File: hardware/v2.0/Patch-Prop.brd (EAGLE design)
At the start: 50 x 28 mm, 49 parts, among them IC1 TPS77033, IC2 XBEE, IC3 MMA8452Q, IC4 ATMEGA168, IC5 MCP1253, IC6 W2RV005RM, U2 MCP73831, X1 USBSMD

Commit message: More small fixes
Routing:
- net GND: track 204.4 -> 234.0 mm
- net VIBE_CONTROL: track 30.5 -> 29.8 mm
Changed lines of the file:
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@@
 <wire x1="44.75" y1="16.2" x2="45.99" y2="14.96" width="0.3048" layer="16"/>
 <wire x1="45.99" y1="14.96" x2="48" y2="14.96" width="0.3048" layer="16"/>
-<wire x1="24.025" y1="11.1" x2="23.6" y2="12.525" width="0" layer="19" extent="16-16"/>
-<wire x1="12.9" y1="20" x2="12.85" y2="20.05" width="0" layer="19" extent="1-16"/>
+<wire x1="8.2" y1="21.7" x2="8.2" y2="19" width="0.3048" layer="1"/>
+<wire x1="8.2" y1="19" x2="8.9" y2="18.3" width="0.3048" layer="1"/>
+<wire x1="8.9" y1="18.3" x2="12.4" y2="18.3" width="0.3048" layer="1"/>
+<wire x1="12.4" y1="18.3" x2="12.9" y2="18.8" width="0.3048" layer="1"/>
+<wire x1="12.9" y1="18.8" x2="12.9" y2="20" width="0.3048" layer="1"/>
+<wire x1="31.2" y1="23.7" x2="15.4" y2="23.7" width="0.3048" layer="1"/>
+<wire x1="15.4" y1="23.7" x2="12.9" y2="21.2" width="0.3048" layer="1"/>
+<wire x1="12.9" y1="21.2" x2="12.9" y2="20" width="0.3048" layer="1"/>
 </signal>
 <signal name="+3V3">
@@
 <wire x1="16.5" y1="26.6" x2="20.3" y2="22.8" width="0.3048" layer="16"/>
 <via x="20.3" y="22.8" extent="1-16" drill="0.5" shape="octagon"/>
-<wire x1="20.3" y1="22.8" x2="20.6" y2="23.1" width="0.3048" layer="1"/>
 <wire x1="29.1" y1="19.9" x2="29.1" y2="22.7" width="0.3048" layer="1"/>
-<wire x1="29.1" y1="22.7" x2="28.4" y2="23.4" width="0.3048" layer="1"/>
-<wire x1="28.4" y1="23.4" x2="20.9" y2="23.4" width="0.3048" layer="1"/>
-<wire x1="20.9" y1="23.4" x2="20.3" y2="22.8" width="0.3048" layer="1"/>
 <wire x1="29.1" y1="19.9" x2="32.9" y2="16.1" width="0.3048" layer="1"/>
 <wire x1="32.9" y1="16.1" x2="32.9" y2="13.7" width="0.3048" layer="1"/>
+<wire x1="29.1" y1="22.7" x2="28.7" y2="23.1" width="0.3048" layer="1"/>
+<wire x1="28.7" y1="23.1" x2="20.6" y2="23.1" width="0.3048" layer="1"/>
+<wire x1="20.6" y1="23.1" x2="20.3" y2="22.8" width="0.3048" layer="1"/>
 </signal>
 <signal name="VIBE">

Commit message: Cleanup
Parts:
- added R10: 4.7k, rcl:R0603
- added R6: RLim, rcl:R0603
- moved R8 17.5 mm to (42.1, 3.40)
- moved R9 15.8 mm to (40.3, 12.9), turned to 270 degrees
- moved C7 5.00 mm to (48.0, 6.00), turned to 270 degrees
- moved T2 2.00 mm to (16.5, 25.5)
- moved SJ2 1.00 mm to (37.2, 5.60), turned to 180 degrees
- moved IC6 0.92 mm to (45.7, 5.40), turned to 270 degrees
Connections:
- new net N$12: IC6.3, R9.1
- new net N$4: R6.2, T2.E
- new net N$7: IC6.1, R8.1
- new net N$9: IC6.2, R10.1
- net +3V3: no longer R8.2, R9.2
- net BLUE: now also R8.2; no longer IC6.1
- net GND: now also R6.1; no longer T2.E
- net GREEN: now also R10.2; no longer IC6.2
- net RED: now also R9.2; no longer IC6.3
- net SCL: no longer R9.1
- net SDA: no longer R8.1
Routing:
- net GND: track 234.0 -> 211.6 mm, vias 7 -> 5
- net RED: track 11.9 -> 4.18 mm
- net BLUE: track 9.66 -> 2.75 mm
- net GREEN: track 9.54 -> 3.45 mm
- net V+: track 81.3 -> 75.9 mm, vias 5 -> 4
- net SDA: track 9.16 -> 5.01 mm
- net N$4: track 0.00 -> 2.87 mm
- net N$1: track 38.3 -> 40.7 mm
- net +3V3: track 132.5 -> 130.4 mm
- net SCL: track 10.7 -> 8.85 mm
- net VIBE: track 9.16 -> 7.45 mm
- net VIBE_CONTROL: track 29.8 -> 28.9 mm

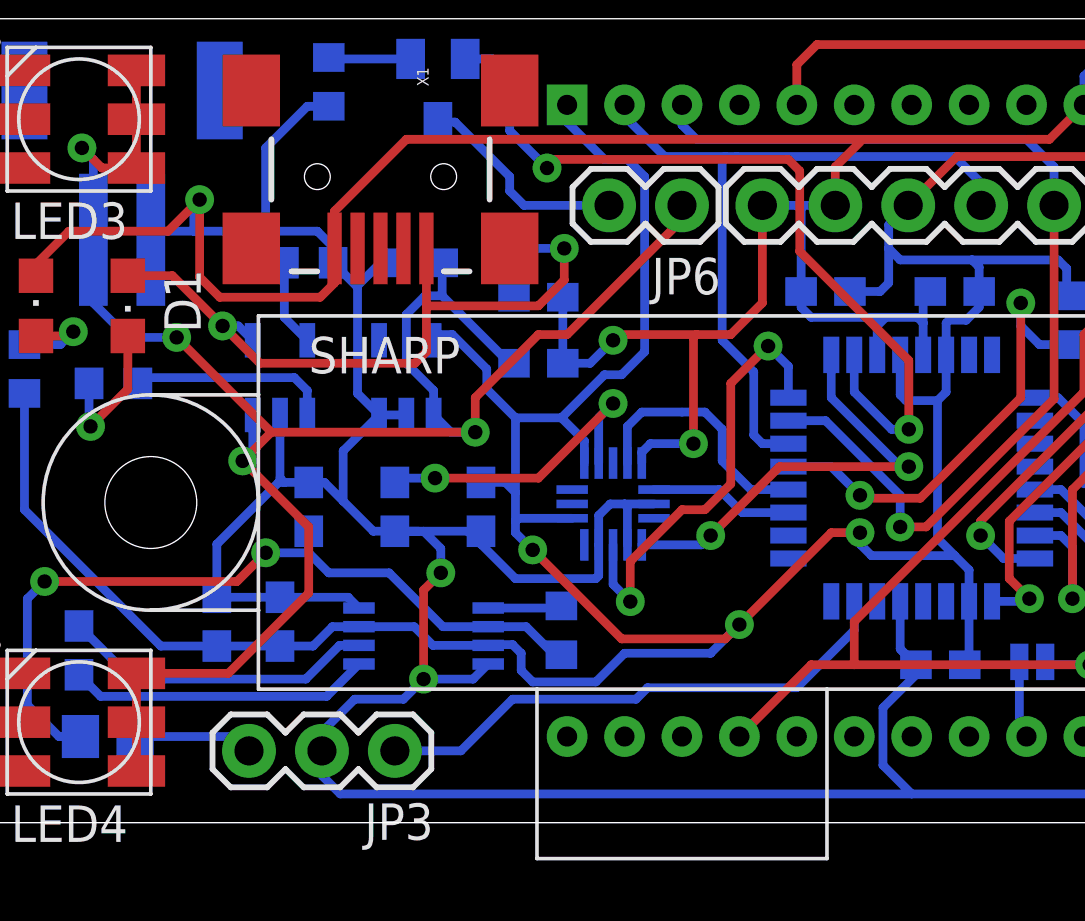
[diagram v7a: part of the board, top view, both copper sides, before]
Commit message: About to move uC
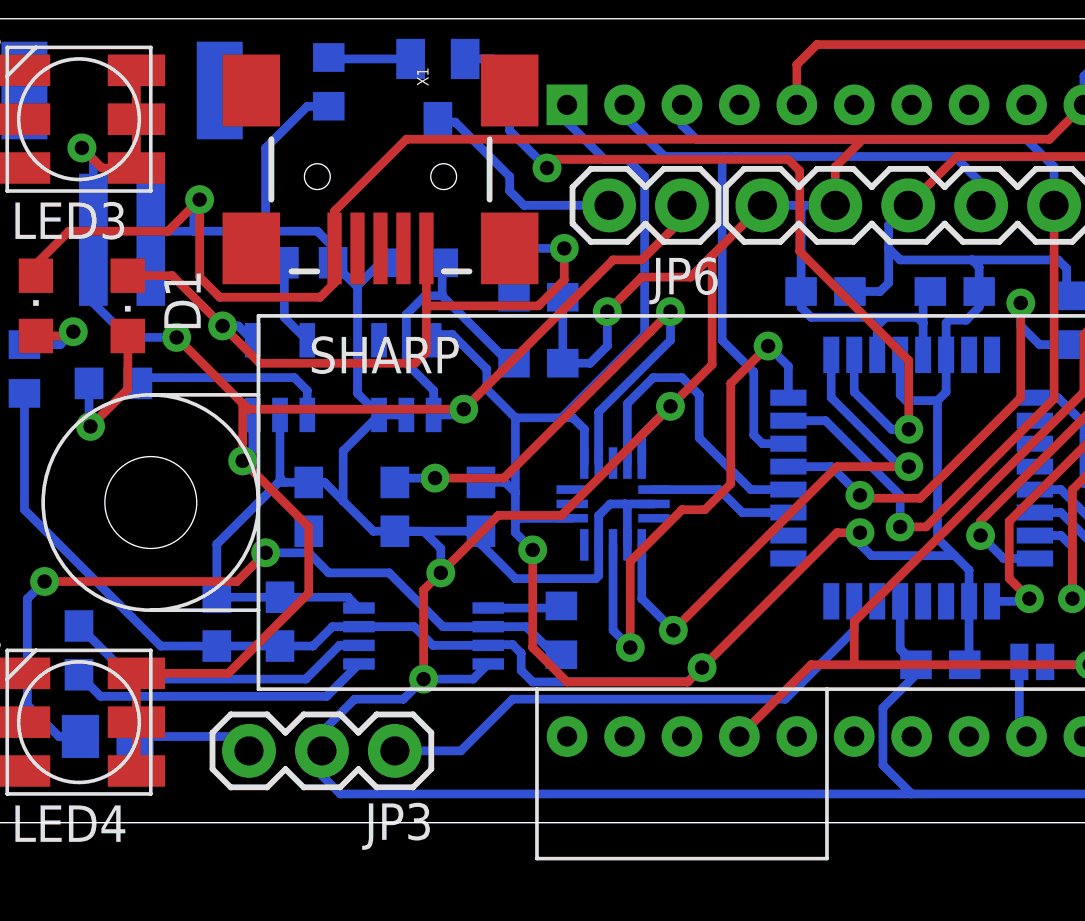
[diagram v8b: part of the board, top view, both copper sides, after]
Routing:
- net GND: track 211.6 -> 222.8 mm
- net N$16: track 11.0 -> 18.4 mm
- net INT1: track 15.6 -> 19.2 mm
- net INT0: track 15.7 -> 18.9 mm
- net SCL: track 8.85 -> 10.5 mm
- net V+: track 75.9 -> 74.5 mm
- net +3V3: track 130.4 -> 131.6 mm
